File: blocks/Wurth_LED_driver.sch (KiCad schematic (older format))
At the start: 0 parts

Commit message: changes on blocks
- added led in power supply
- added wurth led driver
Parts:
- added C? (x2): 2.2u, symbol Device:C
- added VR?: Wurth-LDHM, Package_TO_SOT_SMD:TO-263-7_TabPin4, symbol KTHFS:Wurth-LDHM
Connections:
- new net GND: C?.2, VR?.4 (GND), VR?.6 (Ifix)
- new net LED+: C?.1, C?.1, VR?.1 (LED+), VR?.2 (LED+)
- new net LED-: C?.2, VR?.7 (LED-)
- new net enable: VR?.3 (DIM)
- no-connect marks 0 -> 1
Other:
- note added: "Cin and Cout: X7R"
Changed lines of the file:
@@
 $Descr A4 11693 8268
 encoding utf-8
-Sheet 1 8
+Sheet 4 8
 Title "Schematic Blocks"
 Date "2019-12-05"
@@
 Comment4 ""
 $EndDescr
+$Comp
+L KTHFS:Wurth-LDHM VR?
+U 1 1 5DEA83E7
+P 5375 3475
+F 0 "VR?" H 5375 3990 50  0000 C CNN
+F 1 "Wurth-LDHM" H 5375 3899 50  0000 C CNN
+F 2 "Package_TO_SOT_SMD:TO-263-7_TabPin4" H 5025 3775 50  0001 C CNN
+F 3 "https://katalog.we-online.de/pm/datasheet/172946001.pdf" H 5375 3475 50  0001 C CNN
+	1    5375 3475
+	1    0    0    -1
+$EndComp
+$Comp
+L Device:C C?
+U 1 1 5DEA8676
+P 5975 3550
+F 0 "C?" H 6090 3596 50  0000 L CNN
+F 1 "2.2u" H 6090 3505 50  0000 L CNN
+F 2 "" H 6013 3400 50  0001 C CNN
+F 3 "~" H 5975 3550 50  0001 C CNN
+	1    5975 3550
+	1    0    0    -1
+$EndComp
+Wire Wire Line
+	5775 3325 5975 3325
+Wire Wire Line
+	5975 3325 5975 3400
+Wire Wire Line
+	5775 3775 5975 3775
+Wire Wire Line
+	5975 3775 5975 3700
+Wire Wire Line
+	5775 3225 5975 3225
+Wire Wire Line
+	5975 3225 5975 3325
+Connection ~ 5975 3325
+Text HLabel 7025 3225 2    50   Output ~ 0
+LED+
+Connection ~ 5975 3225
+Text HLabel 7025 3775 2    50   Output ~ 0
+LED-
+Connection ~ 5975 3775
+$Comp
+L power:GND #PWR?
+U 1 1 5DEA8DF3
+P 5375 4150
+F 0 "#PWR?" H 5375 3900 50  0001 C CNN
+F 1 "GND" H 5380 3977 50  0000 C CNN
+F 2 "" H 5375 4150 50  0001 C CNN
+F 3 "" H 5375 4150 50  0001 C CNN
+	1    5375 4150
+	1    0    0    -1
+$EndComp
+Wire Wire Line
+	5375 4150 5375 4075
+$Comp
+L Device:C C?
+U 1 1 5DEA920C
+P 6350 3550
+F 0 "C?" H 6465 3596 50  0000 L CNN
+F 1 "2.2u" H 6465 3505 50  0000 L CNN
+F 2 "" H 6388 3400 50  0001 C CNN
+F 3 "~" H 6350 3550 50  0001 C CNN
+	1    6350 3550
+	1    0    0    -1
+$EndComp
+Wire Wire Line
+	6350 3400 6350 3225
+Connection ~ 6350 3225
+Wire Wire Line
+	6350 3225 5975 3225
+Wire Wire Line
+	6350 3700 6350 4075
+Wire Wire Line
+	6350 4075 5375 4075
+Connection ~ 5375 4075
+Wire Wire Line
+	5375 4075 5375 4025
+Wire Wire Line
+	6350 3225 7025 3225
+Wire Wire Line
+	5975 3775 7025 3775
+Text Notes 6600 3575 0    50   ~ 0
+Cin and Cout: X7R
+Wire Wire Line
+	4975 3775 4800 3775
+Wire Wire Line
+	4800 3775 4800 4075
+Wire Wire Line
+	4800 4075 5375 4075
+NoConn ~ 4975 3675
+Wire Wire Line
+	4975 3225 4125 3225
+Text HLabel 4125 3225 0    50   Input ~ 0
+enable
 $EndSCHEMATC

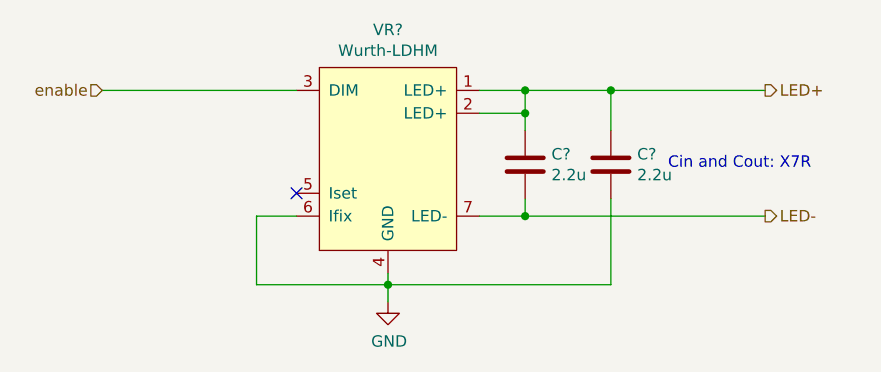
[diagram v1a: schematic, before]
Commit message: added footprints for led driver
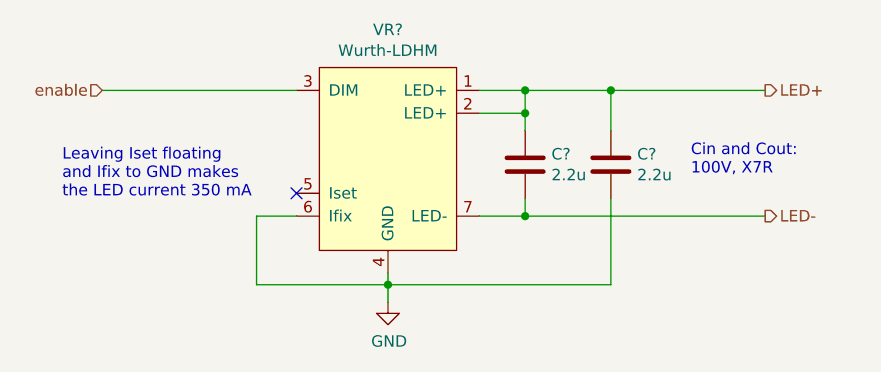
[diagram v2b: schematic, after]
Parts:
- C? (x2): footprint (none) -> Capacitor_SMD:C_1210_3225Metric
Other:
- note added: "Cin and Cout: \n100V, X7R"
- note added: "Leaving Iset floating\nand Ifix to GND makes\nthe LED current 350 mA"
- note removed: "Cin and Cout: X7R"
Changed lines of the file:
@@
 EESchema Schematic File Version 4
-LIBS:blocks-cache
-EELAYER 29 0
+EELAYER 30 0
 EELAYER END
 $Descr A4 11693 8268
@@
 F 0 "C?" H 6090 3596 50  0000 L CNN
 F 1 "2.2u" H 6090 3505 50  0000 L CNN
-F 2 "" H 6013 3400 50  0001 C CNN
+F 2 "Capacitor_SMD:C_1210_3225Metric" H 6013 3400 50  0001 C CNN
 F 3 "~" H 5975 3550 50  0001 C CNN
 	1    5975 3550
@@
 F 0 "C?" H 6465 3596 50  0000 L CNN
 F 1 "2.2u" H 6465 3505 50  0000 L CNN
-F 2 "" H 6388 3400 50  0001 C CNN
+F 2 "Capacitor_SMD:C_1210_3225Metric" H 6388 3400 50  0001 C CNN
 F 3 "~" H 6350 3550 50  0001 C CNN
 	1    6350 3550
@@
 Wire Wire Line
 	5975 3775 7025 3775
-Text Notes 6600 3575 0    50   ~ 0
-Cin and Cout: X7R
+Text Notes 6700 3600 0    50   ~ 0
+Cin and Cout: \n100V, X7R
 Wire Wire Line
 	4975 3775 4800 3775
@@
 Text HLabel 4125 3225 0    50   Input ~ 0
 enable
+Text Notes 3950 3700 0    50   ~ 0
+Leaving Iset floating\nand Ifix to GND makes\nthe LED current 350 mA
 $EndSCHEMATC
